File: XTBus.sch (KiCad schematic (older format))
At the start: 29 parts, among them IC1 74LS157, IC12 74LS139, IC13 74LS245, IC14 D7201C, IC15 D8253C-5, IC2 74LS09, IC3 SN75176AP, IC4 SN75176AP, IC5 74LS123, IC6 74LS393, IC7 74LS14, IC8 74LS04, IC9 74LS11, J1 DB9_Female, J2 Bus_ISA_8bit

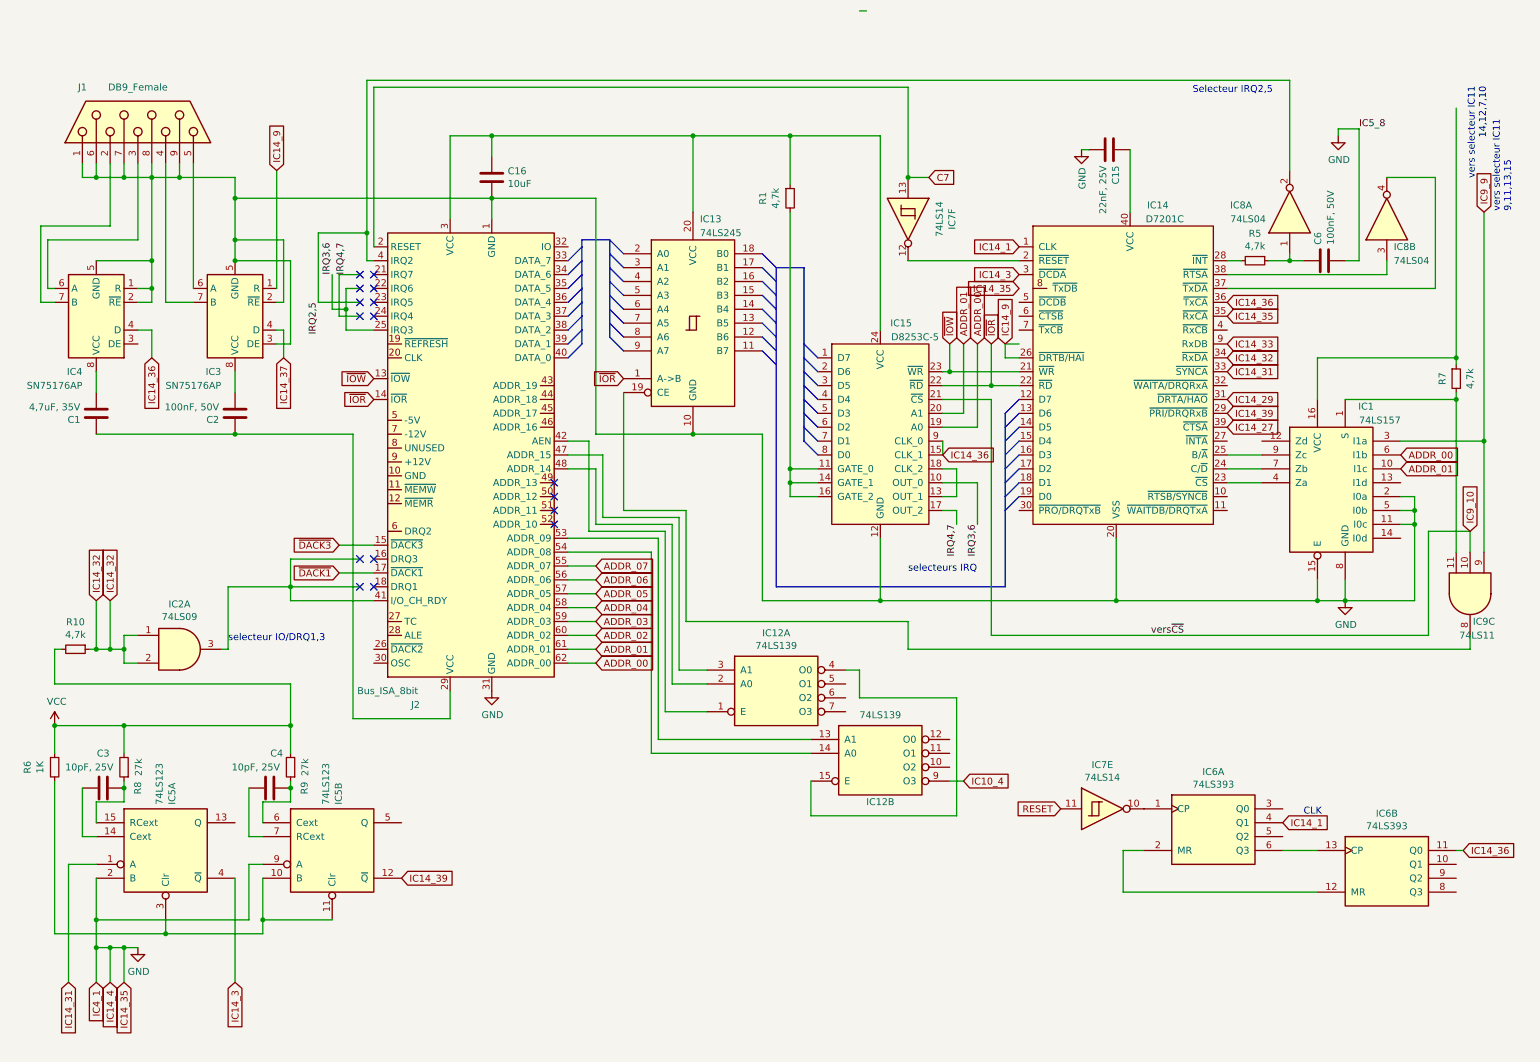
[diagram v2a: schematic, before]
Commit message: Corrections sur IC3 & IC4, nom des pads IC15
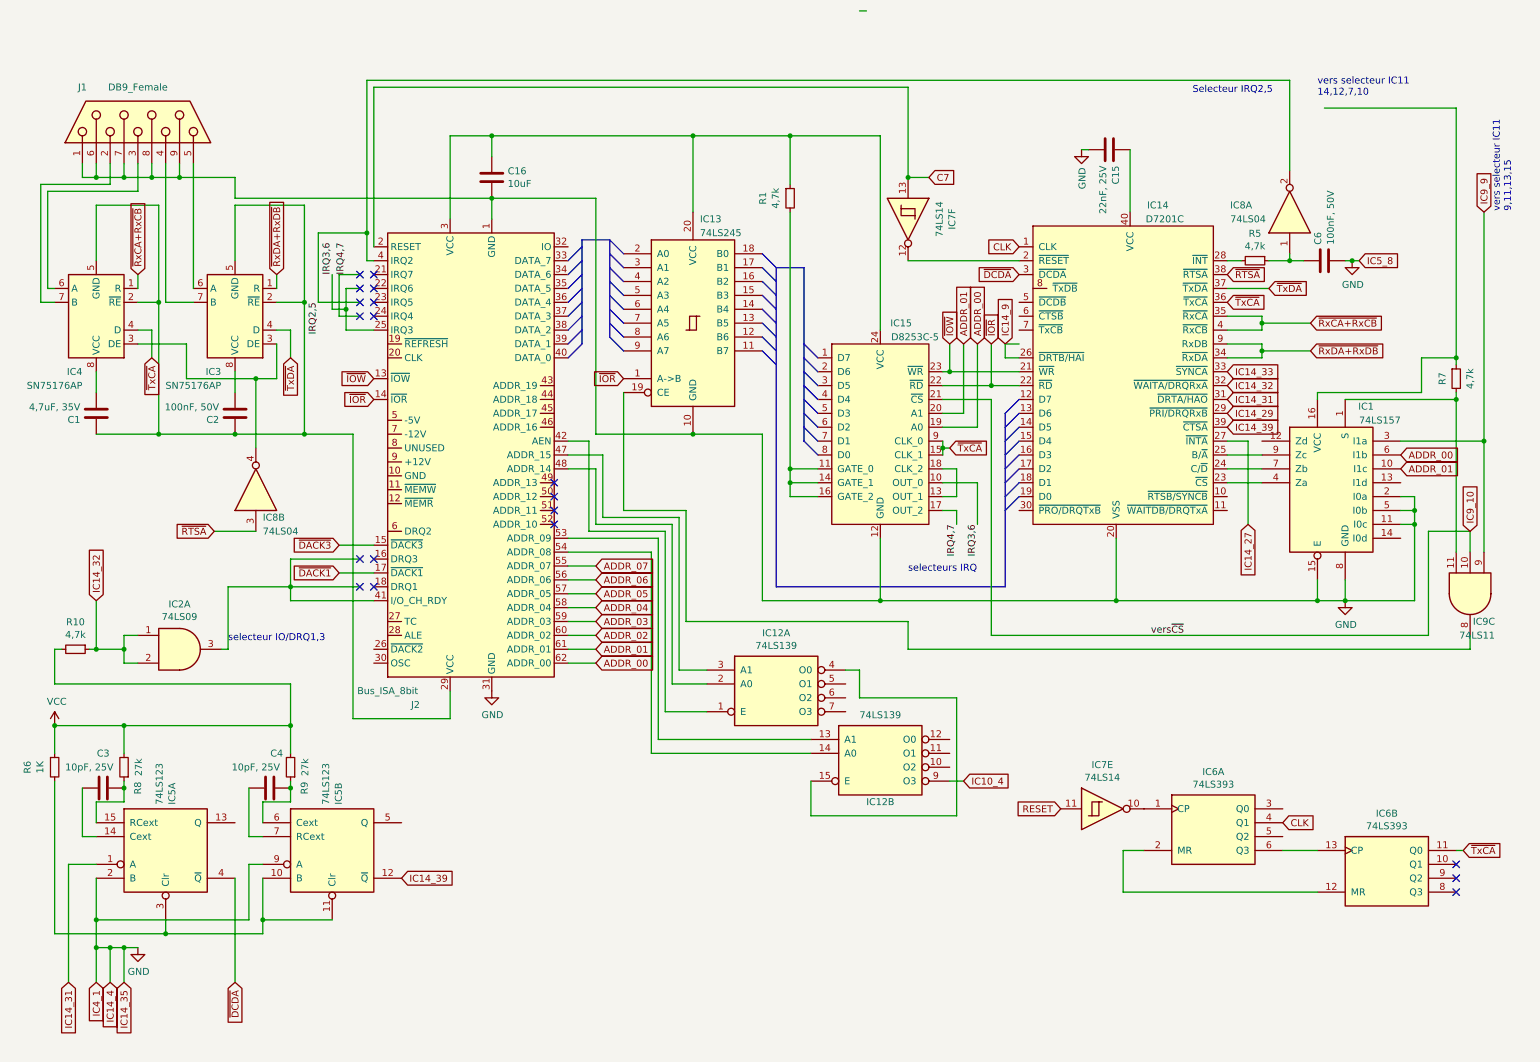
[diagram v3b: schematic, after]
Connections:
- net GND: no longer IC14.35 (~RxCA), IC3.2 (~RE), IC3.3 (DE), IC3.5 (GND), IC4.1 (R), IC4.2 (~RE), IC4.5 (GND)
- net IC14_27: now also IC14.27 (~INTA); no longer IC14.39 (~CTSA)
- net IC14_29: now also IC14.29 (~PRI/DRQRxB); no longer IC14.31 (~DRTA/HAO)
- net IC14_31: now also IC14.31 (~DRTA/HAO); no longer IC14.33 (~SYNCA)
- net IC14_32: now also IC14.32 (~WAITA/DRQRxA); no longer IC14.34 (~RxDA)
- net IC14_33: now also IC14.33 (~SYNCA); no longer IC14.9 (RxDB)
- net IC14_39: now also IC14.39 (~CTSA); no longer IC14.29 (~PRI/DRQRxB)
- net IC14_9: no longer IC3.1 (R)
- net at C1.1, C2.1, J2.29 (VCC): now also IC3.2 (~RE), IC3.5 (GND), IC4.2 (~RE), IC4.5 (GND)
- net at IC8.4: now also IC3.3 (DE), IC4.3 (DE); no longer IC14.37 (~TxDA)
- net ~RTSA: now reaches IC14.38 (~RTSA), IC8.3
- net ~RxCA+RxCB: now reaches IC14.4 (~RxCB)
- net ~RxCA+RxCB: now also IC14.35 (~RxCA), IC4.1 (R)
- net IC14_1 renamed CLK
- net IC14_3 renamed ~DCDA
- net IC14_36 renamed ~TxCA
- net IC14_37 renamed ~TxDA
- net ~TxDA: now also IC14.37 (~TxDA)
- new net ~RxDA+RxDB: IC14.34 (~RxDA), IC14.9 (RxDB), IC3.1 (R)
- no-connect marks 16 -> 19
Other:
- note removed: "CLK"
- moved on the sheet: IC8B
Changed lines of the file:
@@
 L 74xx:74LS04 IC?
 U 2 1 616334FD
-P 10300 1600
+P 2150 3550
 AR Path="/616334FD" Ref="IC?"  Part="2"
 AR Path="/6123EC51/616334FD" Ref="IC?"  Part="2"
 AR Path="/6126F7E9/616334FD" Ref="IC8"  Part="2"
-F 0 "IC8" V 10100 1550 50  0000 R CNN
-F 1 "74LS04" V 10000 1550 50  0000 R CNN
-F 2 "Package_DIP:DIP-14_W7.62mm" H 10300 1600 50  0001 C CNN
-F 3 "http://www.ti.com/lit/gpn/sn74LS04" H 10300 1600 50  0001 C CNN
-	2    10300 1600
+F 0 "IC8" V 1950 3500 50  0000 R CNN
+F 1 "74LS04" V 1850 3500 50  0000 R CNN
+F 2 "Package_DIP:DIP-14_W7.62mm" H 2150 3550 50  0001 C CNN
+F 3 "http://www.ti.com/lit/gpn/sn74LS04" H 2150 3550 50  0001 C CNN
+	2    2150 3550
 	0    -1   -1   0
 $EndComp
@@
 $EndComp
 Wire Wire Line
-	10000 1900 10100 1900
+	10000 1900 10050 1900
 Wire Wire Line
 	9150 1900 9250 1900
-Wire Wire Line
-	9150 2000 10300 2000
 $Comp
 L 74xx:74LS04 IC?
@@
 	10000 2900 10800 2900
 Wire Wire Line
-	9800 2600 9800 2900
-Wire Wire Line
 	10800 2600 10800 2650
-Wire Wire Line
-	9800 2600 10800 2600
 Wire Wire Line
 	10500 3600 10500 3700
@@
 	9600 1900 9700 1900
 Wire Wire Line
-	10300 1900 10300 2000
-Wire Wire Line
-	10300 1300 10650 1300
-Wire Wire Line
-	9150 2100 10650 2100
-Wire Wire Line
 	1200 5450 1200 5250
 Wire Wire Line
@@
 Connection ~ 11000 3200
 Wire Wire Line
-	10650 2100 10650 1300
-Wire Wire Line
 	8150 1100 8100 1100
 Wire Wire Line
@@
 Connection ~ 2000 3150
 Wire Wire Line
-	1000 1900 1400 1900
-Wire Wire Line
 	2000 2700 2000 2850
 Wire Wire Line
 	1000 2700 1000 2850
 Wire Wire Line
-	600  1650 1100 1650
-Wire Wire Line
-	600  2200 600  1650
-Wire Wire Line
 	650  2100 700  2100
 Wire Wire Line
-	650  2100 650  1750
-Wire Wire Line
-	1000 3150 2000 3150
-Wire Wire Line
-	2000 1900 2400 1900
-Connection ~ 2000 1900
+	1000 3150 1450 3150
 Wire Wire Line
 	900  1200 900  1300
 Wire Wire Line
-	1400 2100 1400 2200
-Connection ~ 1400 2100
-Wire Wire Line
-	1300 2100 1400 2100
-Connection ~ 1400 1900
-Wire Wire Line
-	1400 2200 1300 2200
-Wire Wire Line
-	1400 1900 1400 2100
-Wire Wire Line
-	1400 1900 1400 1300
-Wire Wire Line
-	1100 1650 1100 1200
-Wire Wire Line
 	700  2200 600  2200
-Wire Wire Line
-	1300 1750 650  1750
-Wire Wire Line
-	1300 1200 1300 1750
-Connection ~ 2000 1750
-Wire Wire Line
-	2000 1750 2000 1450
-Wire Wire Line
-	2000 1750 2000 1900
 Wire Wire Line
 	1600 1300 2000 1300
@@
 	-1   0    0    1
 $EndComp
-Text GLabel 9150 3100 2    50   Input ~ 0
+Text GLabel 9300 3800 3    50   Input ~ 0
 IC14_27
 Wire Wire Line
@@
 	1500 6750 2200 6750
 Wire Wire Line
-	1000 4700 1100 4700
-Wire Wire Line
 	1200 4700 1200 4800
-Connection ~ 1100 4700
-Wire Wire Line
-	1100 4700 1200 4700
 Wire Wire Line
 	1300 4600 1200 4600
@@
 	1200 4600 1200 4700
 Connection ~ 1200 4700
-Connection ~ 2000 1450
 Wire Wire Line
 	2000 1450 2000 1300
@@
 Wire Wire Line
 	7100 3400 7200 3400
-Text GLabel 9150 2900 2    50   Input ~ 0
+Text GLabel 9150 3000 2    50   Input ~ 0
 IC14_29
 Text GLabel 2000 7100 3    50   Input ~ 0
-IC14_3
+~DCDA
 Wire Wire Line
 	2000 6350 2000 7100
 Text GLabel 7650 2000 0    50   Input ~ 0
-IC14_3
-Text GLabel 2300 1250 1    50   Input ~ 0
-IC14_9
-Wire Wire Line
-	2300 2100 2300 1250
+~DCDA
+Text GLabel 2300 2000 1    50   Input ~ 0
+~RxDA+RxDB
 Text GLabel 7550 2500 1    50   Input ~ 0
 IC14_9
@@
 	950  4700 1000 4700
 Connection ~ 1000 4700
-Text GLabel 9150 2600 2    50   Input ~ 0
+Text GLabel 9150 2800 2    50   Input ~ 0
 IC14_32
-Text GLabel 9150 2700 2    50   Input ~ 0
+Text GLabel 9150 2900 2    50   Input ~ 0
 IC14_31
 Text GLabel 800  7100 3    50   Input ~ 0
@@
 	1200 6850 1200 7100
 Connection ~ 1000 6850
-Text GLabel 9150 2500 2    50   Input ~ 0
+Text GLabel 9150 2700 2    50   Input ~ 0
 IC14_33
 Wire Wire Line
 	1000 6650 2100 6650
-Text GLabel 9150 2300 2    50   Input ~ 0
-IC14_35
 Text GLabel 1100 7100 3    50   Input ~ 0
 IC14_4
@@
 Wire Wire Line
 	1000 6850 1000 7100
-Text GLabel 7100 3300 2    50   Input ~ 0
-IC14_36
+Text GLabel 7150 3250 2    50   Input ~ 0
+~TxCA
 Text GLabel 1400 2600 3    50   Input ~ 0
-IC14_36
-Wire Wire Line
-	1300 2400 1400 2400
-Wire Wire Line
-	1400 2400 1400 2600
-Text GLabel 2350 2600 3    50   Input ~ 0
-IC14_37
-Wire Wire Line
-	2300 2400 2350 2400
-Wire Wire Line
-	2350 2400 2350 2600
+~TxCA
 Text GLabel 9150 2200 2    50   Input ~ 0
-IC14_36
+~TxCA
 Text GLabel 3200 6350 2    50   Input ~ 0
 IC14_39
-Text GLabel 9150 3000 2    50   Input ~ 0
+Text GLabel 9150 3100 2    50   Input ~ 0
 IC14_39
 Wire Wire Line
-	7100 3200 7100 3300
-Text GLabel 7650 2100 0    50   Input ~ 0
-IC14_35
+	7100 3200 7100 3250
 Text GLabel 10850 6150 2    50   Input ~ 0
-IC14_36
+~TxCA
 Text GLabel 7650 1800 0    50   Input ~ 0
-IC14_1
+CLK
 Text GLabel 9550 5950 2    50   Input ~ 0
-IC14_1
-Text Notes 9700 5900 0    50   ~ 0
 CLK
 $Comp
@@
 Connection ~ 5300 3150
 Connection ~ 6650 4350
-Text GLabel 1100 4350 1    50   Input ~ 0
-IC14_32
-Wire Wire Line
-	1100 4350 1100 4700
 Text Notes 1950 4650 0    50   ~ 0
 selecteur IO/DRQ1,3
@@
 Text Notes 11200 1550 1    50   ~ 0
 vers selecteur IC11\n9,11,13,15
-Text Notes 11100 650  3    50   ~ 0
+Text Notes 9800 800  0    50   ~ 0
 vers selecteur IC11\n14,12,7,10\n\n
 Text Label 8600 4600 0    50   ~ 0
@@
 	2750 2000 2900 2000
 Wire Wire Line
-	2350 1750 2350 2200
-Wire Wire Line
-	2300 2200 2350 2200
-Wire Wire Line
-	2350 1750 2000 1750
-Wire Wire Line
-	2400 2500 2400 1900
-Wire Wire Line
-	2400 2500 2300 2500
-Wire Wire Line
 	3000 1900 2950 1900
 NoConn ~ 3000 2000
@@
 Wire Wire Line
 	2600 2200 2600 1700
-Wire Wire Line
-	2000 3150 2850 3150
 Wire Wire Line
 	2850 3150 2850 5200
@@
 L power:GND #PWR?
 U 1 1 61E9BC59
-P 9950 1000
-F 0 "#PWR?" H 9950 750 50  0001 C CNN
-F 1 "GND" H 9955 827 50  0000 C CNN
-F 2 "" H 9950 1000 50  0001 C CNN
-F 3 "" H 9950 1000 50  0001 C CNN
-	1    9950 1000
-	1    0    0    -1
-$EndComp
-Wire Wire Line
-	9950 1000 9950 950
-Wire Wire Line
-	9950 950  10100 950
-Wire Wire Line
-	10100 950  10100 1900
+P 10050 1900
+F 0 "#PWR?" H 10050 1650 50  0001 C CNN
+F 1 "GND" H 10055 1727 50  0000 C CNN
+F 2 "" H 10050 1900 50  0001 C CNN
+F 3 "" H 10050 1900 50  0001 C CNN
+	1    10050 1900
+	1    0    0    -1
+$EndComp
+Wire Wire Line
+	1000 4700 1200 4700
+NoConn ~ 10800 6250
+NoConn ~ 10800 6350
+NoConn ~ 10800 6450
+Wire Wire Line
+	9150 2300 9400 2300
+Wire Wire Line
+	9400 2300 9400 2350
+Wire Wire Line
+	9400 2400 9150 2400
+Wire Wire Line
+	9400 2350 9750 2350
+Connection ~ 9400 2350
+Wire Wire Line
+	9400 2350 9400 2400
+Text GLabel 9750 2350 2    50   Input ~ 0
+~RxCA+RxCB
+Wire Wire Line
+	9300 3200 9300 3800
+Wire Wire Line
+	9150 3200 9300 3200
+Wire Wire Line
+	9150 2500 9400 2500
+Wire Wire Line
+	9400 2500 9400 2550
+Wire Wire Line
+	9400 2600 9150 2600
+Wire Wire Line
+	10550 2600 10550 2850
+Wire Wire Line
+	10550 2850 9800 2850
+Wire Wire Line
+	10550 2600 10800 2600
+Wire Wire Line
+	9800 2850 9800 2900
+Wire Wire Line
+	9400 2550 9750 2550
+Connection ~ 9400 2550
+Wire Wire Line
+	9400 2550 9400 2600
+Text GLabel 9750 2550 2    50   Input ~ 0
+~RxDA+RxDB
+Text GLabel 1300 2000 1    50   Input ~ 0
+~RxCA+RxCB
+Wire Wire Line
+	1450 2200 1450 3150
+Connection ~ 1450 3150
+Wire Wire Line
+	1450 3150 2000 3150
+Wire Wire Line
+	1300 2500 1650 2500
+Wire Wire Line
+	1650 2500 1650 2750
+Wire Wire Line
+	1650 2750 2150 2750
+Wire Wire Line
+	2300 2750 2300 2500
+Wire Wire Line
+	2400 2400 2400 2600
+Wire Wire Line
+	2300 2400 2400 2400
+Wire Wire Line
+	1400 2400 1400 2600
+Wire Wire Line
+	1300 2400 1400 2400
+Wire Wire Line
+	2000 1500 2000 1900
+Wire Wire Line
+	2300 2000 2300 2100
+Connection ~ 1450 2200
+Wire Wire Line
+	1300 2200 1450 2200
+Wire Wire Line
+	1100 1350 600  1350
+Wire Wire Line
+	1100 1350 1100 1200
+Wire Wire Line
+	600  1350 600  2200
+Wire Wire Line
+	650  1400 1300 1400
+Wire Wire Line
+	1300 1200 1300 1400
+Wire Wire Line
+	650  1400 650  2100
+Wire Wire Line
+	1300 2000 1300 2100
+Wire Wire Line
+	1450 1500 1000 1500
+Wire Wire Line
+	1000 1500 1000 1900
+Wire Wire Line
+	1450 1500 1450 2200
+Text GLabel 9450 2100 2    50   Input ~ 0
+~TxDA
+Text GLabel 2400 2600 3    50   Input ~ 0
+~TxDA
+Wire Wire Line
+	7150 3250 7100 3250
+Connection ~ 7100 3250
+Wire Wire Line
+	7100 3250 7100 3300
+Wire Wire Line
+	2150 2750 2150 3250
+Connection ~ 2150 2750
+Wire Wire Line
+	2150 2750 2300 2750
+Text GLabel 1850 3850 0    50   Input ~ 0
+~RTSA
+Wire Wire Line
+	1850 3850 2150 3850
+Text GLabel 9150 2000 2    50   Input ~ 0
+~RTSA
+Wire Wire Line
+	9150 2100 9450 2100
+Text GLabel 10100 1900 2    50   Input ~ 0
+IC5_8
+Connection ~ 10050 1900
+Wire Wire Line
+	10050 1900 10100 1900
+Wire Wire Line
+	10800 800  9850 800
+Wire Wire Line
+	2500 1500 2500 2200
+Connection ~ 2500 3150
+Wire Wire Line
+	2500 3150 2850 3150
 Wire Bus Line
 	4700 1750 4700 2450
@@
 Wire Bus Line
 	7550 3000 7550 4250
-Text Label 10100 950  0    50   ~ 0
-IC5_8
+Connection ~ 2500 2200
+Wire Wire Line
+	2500 2200 2500 3150
+Wire Wire Line
+	2000 1500 2500 1500
+Wire Wire Line
+	2300 2200 2500 2200
+Wire Wire Line
+	2000 3150 2500 3150
 $EndSCHEMATC

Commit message: Schema de Freddy
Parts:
- added IC10, IC11: 74LS138, symbol 74xx:74LS138
- added R4: 4.7k, symbol Device:R
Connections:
- net IC14_29 is gone; now on net GND: IC14.29 (~PRI/DRQRxB)
- net GND: now also IC10.5 (E2), IC10.8 (GND), IC11.5 (E2), IC11.8 (GND); no longer IC5.2 (B), IC5.9 (A)
- net IC14_32: now also R10.2; no longer R10.1
- net VCC: now also C1.1, C16.1, C2.1, IC1.16 (VCC), IC13.20 (VCC), IC15.24 (VCC), IC3.2 (~RE), IC3.5 (GND), IC4.2 (~RE), IC4.5 (GND), J2.29 (VCC), J2.3 (VCC), R1.2, R10.1, R6.2, R7.1, IC10.16 (VCC), IC11.16 (VCC), R4.2; no longer R10.2, R6.1
- net ~RxCA+RxCB: now also IC5.2 (B), IC5.9 (A)
- net at IC5.10 (B), IC5.11 (Clr), IC5.3 (Clr): now also R6.1; no longer R6.2
- net RESET\: now reaches IC14.2 (~RESET), IC7.12
- net at IC1.1 (S), IC9.11, R7.2: now also IC15.21 (~CS)
- net at IC15.11 (GATE_0), IC15.14 (GATE_1), IC15.16 (GATE_2): now also R1.1; no longer R1.2
- net ADDR_00 renamed A0
- net ADDR_01 renamed A1
- net A1: now also IC11.1 (A0)
- net ADDR_02 renamed A2
- net ADDR_03 renamed A3
- net A3: now also IC11.2 (A1)
- net ADDR_04 renamed A4
- net A4: now also IC11.3 (A2)
- net ADDR_05 renamed A5
- net A5: now also IC10.1 (A0)
- net ADDR_06 renamed A6
- net A6: now also IC10.2 (A1)
- net ADDR_07 renamed A7
- net A7: now also IC10.3 (A2)
- net IC10_4 renamed A_3xx
- net A_3xx: now also IC10.4 (E1)
- net IC14_31 renamed DRTA_HAO
- net IC14_39 renamed ~CTSA
- net IC9_10 renamed A_304-307
- net A_304-307: now also IC11.14 (O1); no longer IC15.21 (~CS)
- net IC9_9 renamed A_300-303
- net A_300-303: now also IC11.15 (O0)
- net RESET renamed OSC
- new net: IC10.15 (O0), IC11.4 (E1)
- new net: IC10.6 (E3), IC11.6 (E3), R4.1
- no-connect marks 19 -> 54
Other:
- note added: "0 For IO @ 300 to 307"
- note added: "Bizarre VCC en direct vers des pin de \nsignaux sur IC3 IC4"
- note added: "Clock Divisor"
- note added: "vers selecteur DACK 1,2,3\n\n"
- note removed: "vers selecteur IC11\n14,12,7,10\n\n"
- moved on the sheet: C3, C4, IC12A, IC12B, IC15, IC2A, IC5A, IC5B, IC6A, IC6B, IC7E, IC7F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

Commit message: Dernière version de Freddy
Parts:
- added R3: 4.7K, symbol Device:R
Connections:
- net A_304-307: now also IC15.21 (~CS)
- net GND: now also C1.1, C2.1, IC3.2 (~RE), IC3.5 (GND), IC4.2 (~RE), IC4.5 (GND)
- net IRQ3,6: no longer J2.25 (IRQ3)
- net VCC: now also C1.2, C2.2, C6.1, IC4.8 (VCC), R5.1, R3.2; no longer C1.1, C2.1, IC3.2 (~RE), IC3.5 (GND), IC4.2 (~RE), IC4.5 (GND)
- net at IC14.28 (~INT), R5.2: now also IC8.1
- net DACK1_3: now reaches IC1.1 (S), IC9.11, R7.2
- net DACK1_3: no longer IC15.21 (~CS)
- net at IC3.8 (VCC): no longer C2.2
- net DRTA_HAO renamed DTRA_HAO
- net IC14_27: no longer names the net of IC14.27 (~INTA)
- net IC14_27: now also R3.1
- net IC14_32 renamed WAITA\
- net IC14_9: no longer names the net of IC14.26 (~DRTB/HAI)
- net IRQ2,5 renamed IRQ2_5
- new net IRQ3_6: J2.25 (IRQ3)
- no-connect marks 54 -> 59
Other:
- note added: "Add delay to the IO Read/Write"
- note added: "CLK=OSC/4\nTxCA=CLK/2=OSC/8=1.75MHz"
- note added: "CTSA\ is Low when there is no Input clock.\n-> The PC can send data"
- note added: "Filtrage\nIC14"
- note added: "Selecteur DRQ1,3"
- note added: "When DTRA\ is Low, DCDA is High\nwhen a Clock is received.\nWhen DRTA is High, DCDA\ is High"
- note added: "Za,b,c copy Ia,b,c except if S=0"
- note removed: "Selecteur IRQ2,5"
- note removed: "selecteur IO/DRQ1,3"
- note removed: "selecteurs IRQ"
- note removed: "vers selecteur DACK 1,2,3\n\n"
- moved on the sheet: C1, C2, C6, IC8A, IC8B, R5
